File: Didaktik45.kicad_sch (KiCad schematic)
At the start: 102 parts, among them J1 USB_C_Receptacle_USB2.0, SW1 SW_Push, SW10 SW_Push_45deg, SW11 SW_Push_45deg, SW12 SW_Push_45deg, SW13 SW_Push_45deg, SW14 SW_Push_45deg, SW15 SW_Push_45deg, SW16 SW_Push_45deg, SW17 SW_Push_45deg, SW18 SW_Push_45deg, SW19 SW_Push_45deg, SW2 SW_Push_45deg, SW20 SW_Push_45deg, SW21 SW_Push_45deg, SW22 SW_Push_45deg, SW23 SW_Push_45deg, SW24 SW_Push_45deg, SW25 SW_Push_45deg, SW26 SW_Push_45deg, SW27 SW_Push_45deg, SW28 SW_Push_45deg, SW29 SW_Push_45deg, SW3 SW_Push_45deg, SW30 SW_Push_45deg, SW31 SW_Push_45deg, SW32 SW_Push_45deg, SW33 SW_Push_45deg, SW34 SW_Push_45deg, SW35 SW_Push_45deg, SW36 SW_Push_45deg, SW37 SW_Push_45deg, SW38 SW_Push_45deg, SW39 SW_Push_45deg, SW4 SW_Push_45deg, SW40 SW_Push_45deg, SW41 SW_Push_45deg, SW5 SW_Push_45deg, SW6 SW_Push_45deg, SW7 SW_Push_45deg, SW8 SW_Push_45deg, SW9 SW_Push_45deg, U1 ATmega32U4-M, Y1 Crystal_GND24_Small

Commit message: initial commit
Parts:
- added D? (x5): D_Small, symbol ComboDiode:D_Small
- added SW? (x5): SW_Push_45deg, symbol Switch:SW_Push_45deg
- C?: renamed from C9; footprint Capacitor_SMD:C_0402_1005Metric -> (none)
- C?: renamed from C4; footprint Capacitor_SMD:C_0402_1005Metric -> (none)
- C?: renamed from C6; footprint Capacitor_SMD:C_0402_1005Metric -> (none)
- C?: renamed from C1; footprint Capacitor_SMD:C_0402_1005Metric -> (none)
- C?: renamed from C3; footprint Capacitor_SMD:C_0402_1005Metric -> (none)
- C?: renamed from C2; footprint Capacitor_SMD:C_0402_1005Metric -> (none)
- C?: renamed from C8; footprint Capacitor_SMD:C_0402_1005Metric -> (none)
- C?: renamed from C7; footprint Capacitor_SMD:C_0402_1005Metric -> (none)
- C?: renamed from C5; footprint Capacitor_SMD:C_0402_1005Metric -> (none)
- D?: renamed from D28; footprint combodiode:ComboDiode -> (none)
- D?: renamed from D17; footprint combodiode:ComboDiode -> (none)
- D?: renamed from D3; footprint combodiode:ComboDiode -> (none)
- D?: renamed from D7; footprint combodiode:ComboDiode -> (none)
- D?: renamed from D37; footprint combodiode:ComboDiode -> (none)
- D?: renamed from D8; footprint combodiode:ComboDiode -> (none)
- D?: renamed from D33; footprint combodiode:ComboDiode -> (none)
- D?: renamed from D34; footprint combodiode:ComboDiode -> (none)
- D?: renamed from D20; footprint combodiode:ComboDiode -> (none)
- D?: renamed from D24; footprint combodiode:ComboDiode -> (none)
- D?: renamed from D14; footprint combodiode:ComboDiode -> (none)
- D?: renamed from D13; footprint combodiode:ComboDiode -> (none)
- D?: renamed from D15; footprint combodiode:ComboDiode -> (none)
- D?: renamed from D16; footprint combodiode:ComboDiode -> (none)
- D?: renamed from D22; footprint combodiode:ComboDiode -> (none)
- D?: renamed from D36; footprint combodiode:ComboDiode -> (none)
- D?: renamed from D26; footprint combodiode:ComboDiode -> (none)
- D?: renamed from D41; footprint combodiode:ComboDiode -> (none)
- D?: renamed from D12; footprint combodiode:ComboDiode -> (none)
- D?: renamed from D18; footprint combodiode:ComboDiode -> (none)
- D?: renamed from D40; footprint combodiode:ComboDiode -> (none)
- D?: renamed from D21; footprint combodiode:ComboDiode -> (none)
- D?: renamed from D5; footprint combodiode:ComboDiode -> (none)
- D?: renamed from D29; footprint combodiode:ComboDiode -> (none)
- D?: renamed from D10; footprint combodiode:ComboDiode -> (none)
- D?: renamed from D27; footprint combodiode:ComboDiode -> (none)
- D?: renamed from D2; footprint combodiode:ComboDiode -> (none)
- D?: renamed from D32; footprint combodiode:ComboDiode -> (none)
- D?: renamed from D31; footprint combodiode:ComboDiode -> (none)
- D?: renamed from D23; footprint combodiode:ComboDiode -> (none)
- D?: renamed from D4; footprint combodiode:ComboDiode -> (none)
- D?: renamed from D1; footprint combodiode:ComboDiode -> (none)
- D?: renamed from D9; footprint combodiode:ComboDiode -> (none)
- D?: renamed from D30; footprint combodiode:ComboDiode -> (none)
- D?: renamed from D38; footprint combodiode:ComboDiode -> (none)
- D?: renamed from D11; footprint combodiode:ComboDiode -> (none)
- D?: renamed from D39; footprint combodiode:ComboDiode -> (none)
- D?: renamed from D6; footprint combodiode:ComboDiode -> (none)
- D?: renamed from D19; footprint combodiode:ComboDiode -> (none)
- D?: renamed from D35; footprint combodiode:ComboDiode -> (none)
- F?: renamed from F1; footprint Fuse:Fuse_1206_3216Metric -> (none)
- J?: renamed from J1; footprint Connector_USB:USB_C_Receptacle_HRO_TYPE-C-31-M-12 -> (none)
- R?: renamed from R1; footprint Resistor_SMD:R_0402_1005Metric -> (none)
- R?: renamed from R6; footprint Resistor_SMD:R_0402_1005Metric -> (none)
- R?: renamed from R3; footprint Resistor_SMD:R_0402_1005Metric -> (none)
- R?: renamed from R4; footprint Resistor_SMD:R_0402_1005Metric -> (none)
- R?: renamed from R5; footprint Resistor_SMD:R_0402_1005Metric -> (none)
- R?: renamed from R7; footprint Resistor_SMD:R_0402_1005Metric -> (none)
- R?: renamed from R2; footprint Resistor_SMD:R_0402_1005Metric -> (none)
- SW?: renamed from SW9; footprint Keebio-Parts:MX-Alps-Choc-1U-NoLED -> (none)
- SW?: renamed from SW36; footprint Keebio-Parts:MX-Alps-Choc-1U-NoLED -> (none)
- SW?: renamed from SW2; footprint Keebio-Parts:MX-Alps-Choc-1U-NoLED -> (none)
- SW?: renamed from SW12; footprint Keebio-Parts:MX-Alps-Choc-1U-NoLED -> (none)
- SW?: renamed from SW1; footprint random-keyboard-parts:SKQG-1155865 -> (none)
- SW?: renamed from SW15; footprint Keebio-Parts:MX-Alps-Choc-1U-NoLED -> (none)
- SW?: renamed from SW41; footprint Keebio-Parts:MX-Alps-Choc-1U-NoLED -> (none)
- SW?: renamed from SW13; footprint Keebio-Parts:MX-Alps-Choc-1U-NoLED -> (none)
- SW?: renamed from SW29; footprint Keebio-Parts:MX-Alps-Choc-1U-NoLED -> (none)
- SW?: renamed from SW38; footprint Keebio-Parts:MX-Alps-Choc-1U-NoLED -> (none)
- SW?: renamed from SW35; footprint Keebio-Parts:MX-Alps-Choc-1U-NoLED -> (none)
- SW?: renamed from SW21; footprint Keebio-Parts:MX-Alps-Choc-1U-NoLED -> (none)
- SW?: renamed from SW32; footprint Keebio-Parts:MX-Alps-Choc-1U-NoLED -> (none)
- SW?: renamed from SW10; footprint Keebio-Parts:MX-Alps-Choc-1U-NoLED -> (none)
- SW?: renamed from SW34; footprint Keebio-Parts:MX-Alps-Choc-1U-NoLED -> (none)
- SW?: renamed from SW33; footprint Keebio-Parts:MX-Alps-Choc-1U-NoLED -> (none)
- SW?: renamed from SW11; footprint Keebio-Parts:MX-Alps-Choc-1U-NoLED -> (none)
- SW?: renamed from SW22; footprint Keebio-Parts:MX-Alps-Choc-1U-NoLED -> (none)
- SW?: renamed from SW27; footprint Keebio-Parts:MX-Alps-Choc-1U-NoLED -> (none)
- SW?: renamed from SW7; footprint Keebio-Parts:MX-Alps-Choc-1U-NoLED -> (none)
- SW?: renamed from SW6; footprint Keebio-Parts:MX-Alps-Choc-1U-NoLED -> (none)
- SW?: renamed from SW40; footprint Keebio-Parts:MX-Alps-Choc-1U-NoLED -> (none)
- SW?: renamed from SW3; footprint Keebio-Parts:MX-Alps-Choc-1U-NoLED -> (none)
- SW?: renamed from SW18; footprint Keebio-Parts:MX-Alps-Choc-1U-NoLED -> (none)
- SW?: renamed from SW23; footprint Keebio-Parts:MX-Alps-Choc-1U-NoLED -> (none)
- SW?: renamed from SW16; footprint Keebio-Parts:MX-Alps-Choc-1U-NoLED -> (none)
- SW?: renamed from SW25; footprint Keebio-Parts:MX-Alps-Choc-1U-NoLED -> (none)
- SW?: renamed from SW24; footprint Keebio-Parts:MX-Alps-Choc-1U-NoLED -> (none)
- SW?: renamed from SW5; footprint Keebio-Parts:MX-Alps-Choc-1U-NoLED -> (none)
- SW?: renamed from SW14; footprint Keebio-Parts:MX-Alps-Choc-1U-NoLED -> (none)
- SW?: renamed from SW20; footprint Keebio-Parts:MX-Alps-Choc-1U-NoLED -> (none)
- SW?: renamed from SW8; footprint Keebio-Parts:MX-Alps-Choc-1U-NoLED -> (none)
- SW?: renamed from SW37; footprint Keebio-Parts:MX-Alps-Choc-1U-NoLED -> (none)
- SW?: renamed from SW31; footprint Keebio-Parts:MX-Alps-Choc-1U-NoLED -> (none)
- SW?: renamed from SW26; footprint Keebio-Parts:MX-Alps-Choc-1U-NoLED -> (none)
- SW?: renamed from SW4; footprint Keebio-Parts:MX-Alps-Choc-1U-NoLED -> (none)
- SW?: renamed from SW17; footprint Keebio-Parts:MX-Alps-Choc-1U-NoLED -> (none)
- SW?: renamed from SW39; footprint Keebio-Parts:MX-Alps-Choc-1U-NoLED -> (none)
- SW?: renamed from SW28; footprint Keebio-Parts:MX-Alps-Choc-1U-NoLED -> (none)
- SW?: renamed from SW30; footprint Keebio-Parts:MX-Alps-Choc-1U-NoLED -> (none)
- SW?: renamed from SW19; footprint Keebio-Parts:MX-Alps-Choc-1U-NoLED -> (none)
- Y?: renamed from Y1; footprint Crystal:Crystal_SMD_3225-4Pin_3.2x2.5mm -> (none)
- renumbered D25 to D?, U1 to U?
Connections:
- net ROW0: now also D?.1 (K)
- net ROW4: now also D?.1 (K)
- net ROW6: now also D?.1 (K), D?.1 (K)
- net ROW7: now also D?.1 (K)
- new net: D?.2 (A), SW?.2 (x5)
- new net COL5: SW?.1, SW?.1, SW?.1
- new net COL6: SW?.1, SW?.1
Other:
- note added: "Didaktik 45"
- note added: "MISSING ONE POWER LED"
- note removed: "CAPS?"
- note removed: "Didaktik 40"
- note removed: "POWER"
- note removed: "RESET BUTTON"

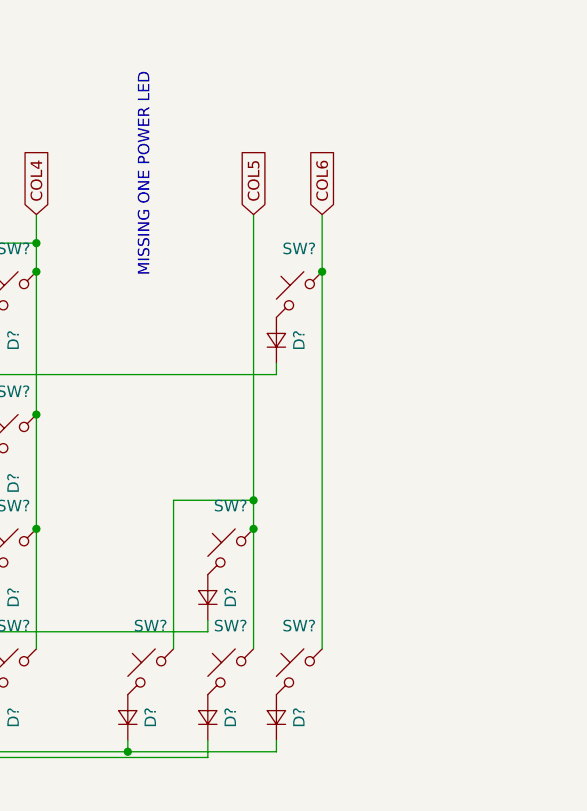
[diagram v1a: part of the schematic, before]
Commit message: switch placement done, basic matrix routing done
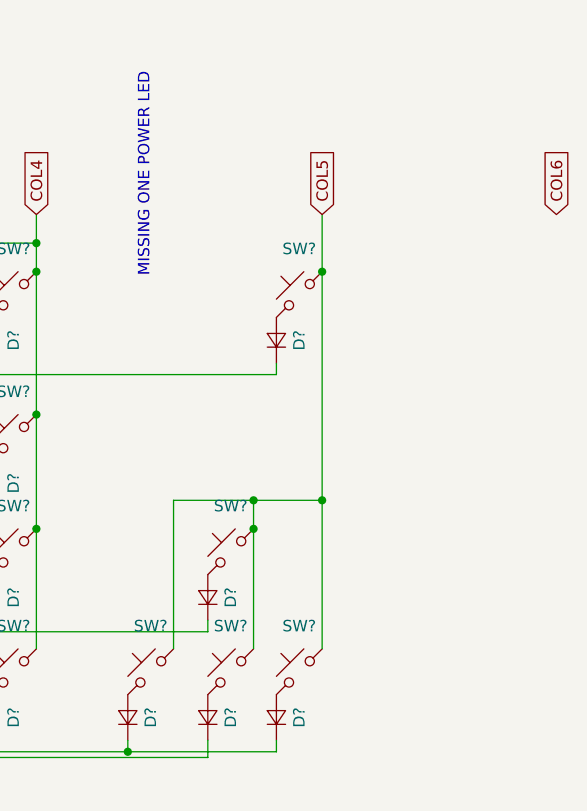
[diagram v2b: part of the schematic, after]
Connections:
- net COL5: now also SW?.1, SW?.1
- net COL6: no longer SW?.1, SW?.1
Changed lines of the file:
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@@
   (junction (at 27.94 158.75) (diameter 0) (color 0 0 0 0)
   )
+  (junction (at 203.2 69.85) (diameter 0) (color 0 0 0 0)
+  )
   (junction (at 114.3 60.325) (diameter 0) (color 0 0 0 0)
   )
@@
   (junction (at 146.05 73.025) (diameter 0) (color 0 0 0 0)
   )
+  (junction (at 195.58 69.85) (diameter 0) (color 0 0 0 0)
+  )
   (junction (at 147.32 55.88) (diameter 0) (color 0 0 0 0)
   )
@@
   (junction (at 146.05 41.275) (diameter 0) (color 0 0 0 0)
   )
-  (junction (at 195.58 69.85) (diameter 0) (color 0 0 0 0)
-  )
   (junction (at 152.4 60.325) (diameter 0) (color 0 0 0 0)
   )
@@
     (stroke (width 0) (type default) (color 0 0 0 0))
   )
-  (wire (pts (xy 203.2 44.45) (xy 203.2 86.36))
+  (wire (pts (xy 203.2 44.45) (xy 203.2 69.85))
     (stroke (width 0) (type default) (color 0 0 0 0))
   )
@@
     (stroke (width 0) (type default) (color 0 0 0 0))
   )
+  (wire (pts (xy 195.58 69.85) (xy 203.2 69.85))
+    (stroke (width 0) (type default) (color 0 0 0 0))
+  )
   (wire (pts (xy 140.97 71.755) (xy 153.67 71.755))
     (stroke (width 0) (type default) (color 0 0 0 0))
@@
     (stroke (width 0) (type default) (color 0 0 0 0))
   )
-  (wire (pts (xy 195.58 38.1) (xy 195.58 69.85))
-    (stroke (width 0) (type default) (color 0 0 0 0))
-  )
   (wire (pts (xy 105.41 71.755) (xy 105.41 73.66))
     (stroke (width 0) (type default) (color 0 0 0 0))
@@
   )
   (wire (pts (xy 116.84 143.51) (xy 120.65 143.51))
+    (stroke (width 0) (type default) (color 0 0 0 0))
+  )
+  (wire (pts (xy 203.2 69.85) (xy 203.2 86.36))
     (stroke (width 0) (type default) (color 0 0 0 0))
   )
@@
     )
   )
-  (global_label "COL6" (shape input) (at 203.2 38.1 90) (fields_autoplaced)
+  (global_label "COL6" (shape input) (at 229.235 38.1 90) (fields_autoplaced)
     (effects (font (size 1.27 1.27)) (justify left))
-    (property "Intersheet References" "${INTERSHEET_REFS}" (id 0) (at 203.1206 30.8488 90)
+    (property "Intersheet References" "${INTERSHEET_REFS}" (id 0) (at 229.1556 30.8488 90)
       (effects (font (size 1.27 1.27)) (justify left) hide)
     )
@@
     )
   )
-  (global_label "COL5" (shape input) (at 195.58 38.1 90) (fields_autoplaced)
+  (global_label "COL5" (shape input) (at 203.2 38.1 90) (fields_autoplaced)
     (effects (font (size 1.27 1.27)) (justify left))
-    (property "Intersheet References" "${INTERSHEET_REFS}" (id 0) (at 195.5006 30.8488 90)
+    (property "Intersheet References" "${INTERSHEET_REFS}" (id 0) (at 203.1206 30.8488 90)
       (effects (font (size 1.27 1.27)) (justify left) hide)
     )

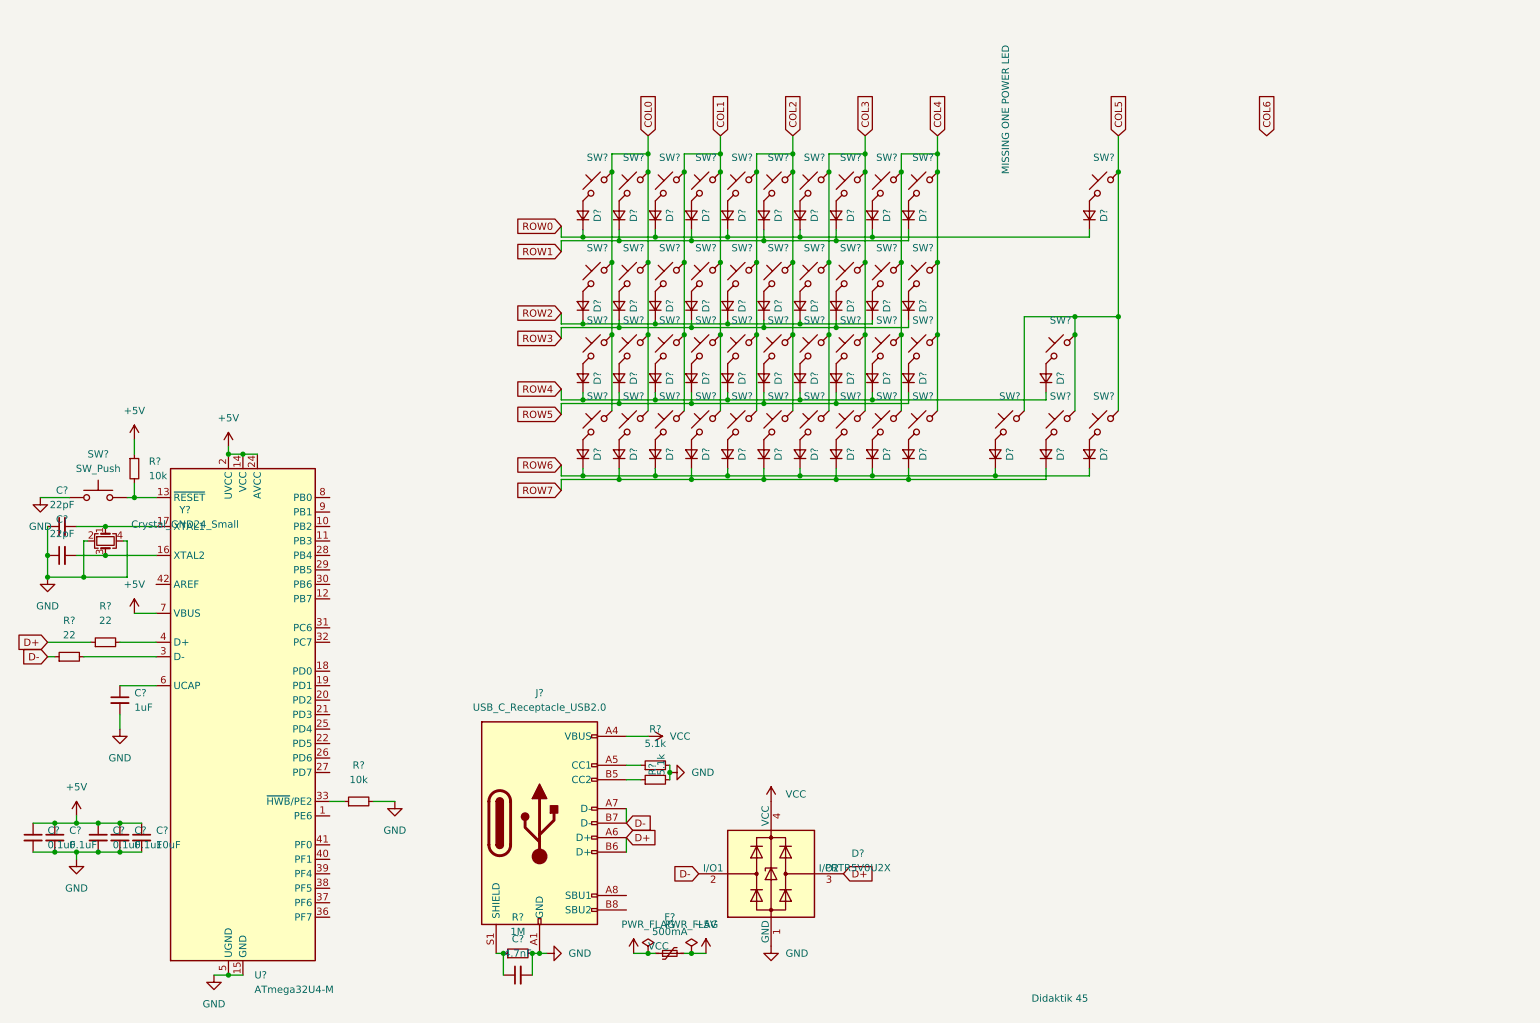
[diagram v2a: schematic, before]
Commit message: created switchplate 40, cleaned 40s pcb. finished schematics for 45. created pcb project for 45
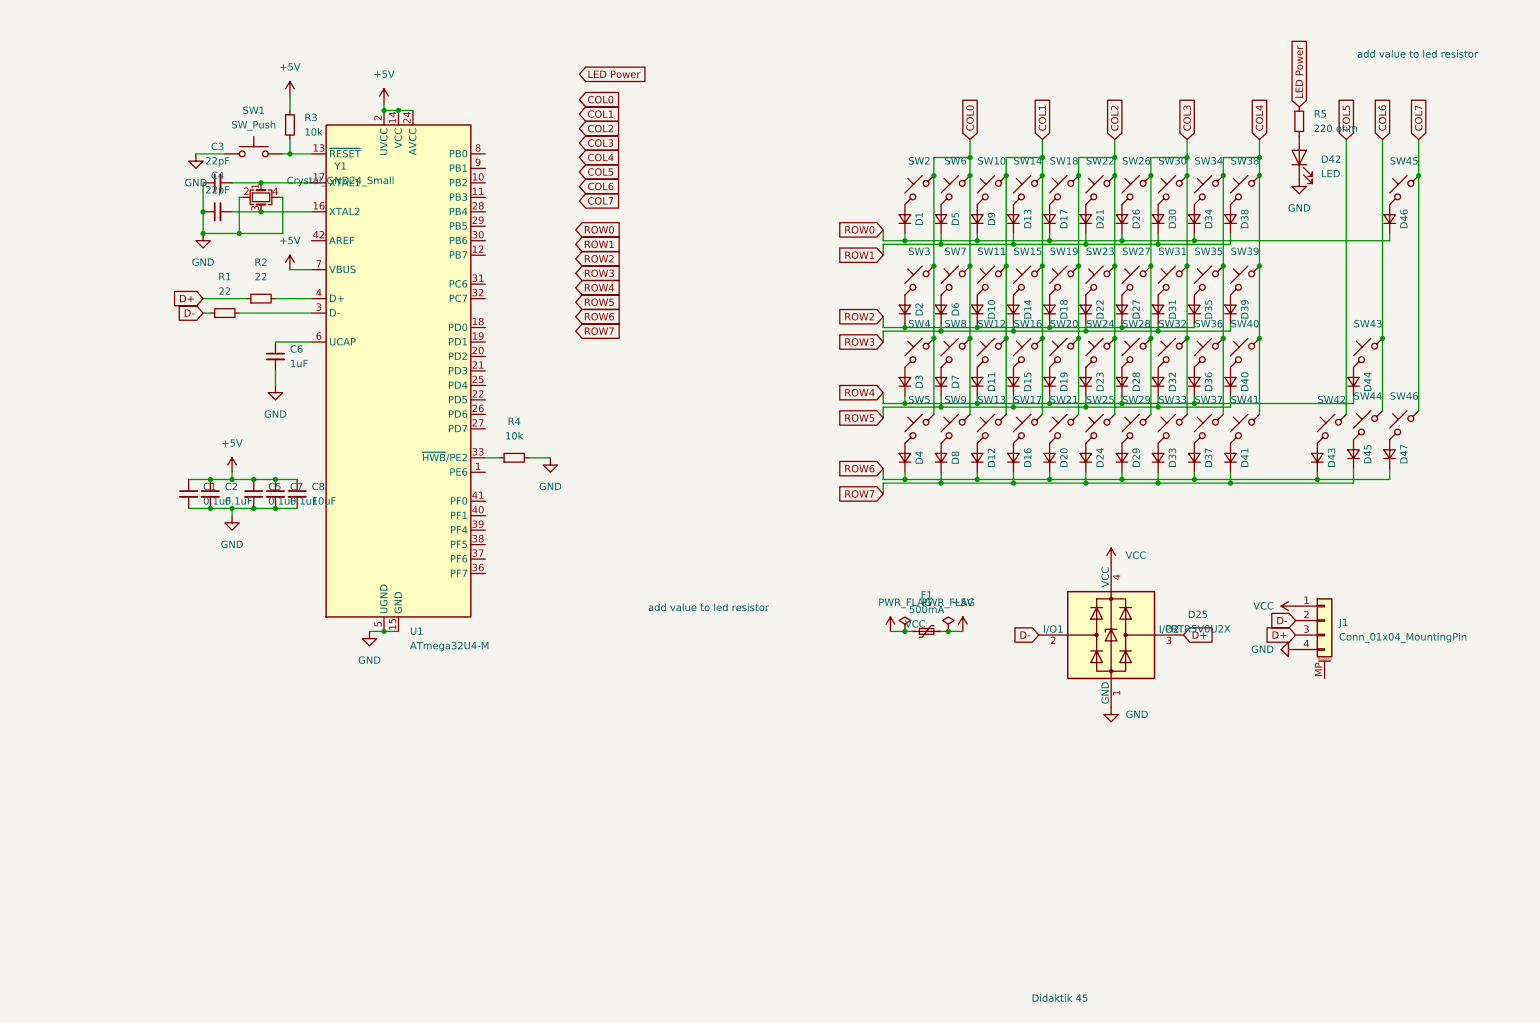
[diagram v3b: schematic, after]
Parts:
- removed C?: 4.7nF, symbol ComboDiode:C_Small
- removed J?: USB_C_Receptacle_USB2.0, symbol Connector:USB_C_Receptacle_USB2.0
- removed R? (x2): 5.1k, symbol ComboDiode:R_Small
- removed R?: 1M, symbol ComboDiode:R_Small
- added D42: LED, Keebio-Parts:LED_3mm, symbol ComboDiode:LED
- added J1: Conn_01x04_MountingPin, random-keyboard-parts:JST-SR-4, symbol Connector_Generic_MountingPin:Conn_01x04_MountingPin
- added R5: 220 ohm, Resistor_SMD:R_0402_1005Metric, symbol ComboDiode:R_Small
- C1, C2, C3, C4, C5, C6, C7, C8: renamed from C?; footprint (none) -> Capacitor_SMD:C_0402_1005Metric
- D1, D10, D11, D12, D13, D14, D15, D16, D17, D18, D19, D2, D20, D21, D22, D23, D24, D26, D27, D28, D29, D3, D30, D31, D32, D33, D34, D35, D36, D37, D38, D39, D4, D40, D41, D43, D44, D45, D46, D47, D5, D6, D7, D8, D9: renamed from D?; footprint (none) -> Diode_SMD:D_SOD-123
- F1: renamed from F?; footprint (none) -> Fuse:Fuse_1206_3216Metric
- R1, R2, R3, R4: renamed from R?; footprint (none) -> Resistor_SMD:R_0402_1005Metric
- SW1: renamed from SW?; footprint (none) -> random-keyboard-parts:SKQG-1155865
- SW10, SW11, SW12, SW13, SW14, SW15, SW16, SW17, SW18, SW19, SW2, SW20, SW21, SW22, SW23, SW24, SW25, SW26, SW27, SW28, SW29, SW3, SW30, SW31, SW32, SW33, SW34, SW35, SW36, SW37, SW38, SW39, SW4, SW40, SW41, SW42, SW43, SW44, SW45, SW46, SW5, SW6, SW7, SW8, SW9: renamed from SW?; footprint (none) -> Keebio-Parts:MX-Alps-Choc-1U-NoLED
- Y1: renamed from Y?; footprint (none) -> Crystal:Crystal_SMD_3225-4Pin_3.2x2.5mm
- gave numbers to parts that had none: 2
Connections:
- net COL5: no longer SW43.1, SW44.1, SW45.1, SW46.1
- net COL6: now also SW43.1, SW44.1
- net D+: now also J1.3 (Pin_3)
- net D-: now also J1.2 (Pin_2)
- net GND: now also D42.1 (K), J1.4 (Pin_4)
- net VCC: now also J1.1 (Pin_1)
- new net: D42.2 (A), R5.2
- new net COL7: SW45.1, SW46.1
- new net LED Power: R5.1
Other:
- note added: "add value to led resistor"
- note removed: "MISSING ONE POWER LED"
- moved on the sheet: C1, C2, C3, C4, C5, C6, C7, C8, D1, D10, D11, D12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
